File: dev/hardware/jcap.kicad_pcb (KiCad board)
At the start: 2 copper layers, 136.8 x 87 mm, 65 parts, among them J201 CPU PGMR, J202 SPARE CPU HDR, J203 GPU PGMR, J204 SPARE GPU HDR, J301 DC IN, J501 VGA OUT, J601 CONTROLS, Q301 IPP80P03P4L-04, SW201 CPU ~{RES}, SW202 DEBUG, SW203 GPU ~{RES}, SW601 TILT, U201 P8X32A-D40, U202 P8X32A-D40, U301 LF33_TO220, U401 24LC256, U402 24LC256, U601 74HC165, U602 74HC165, Y201 6.5MHz, Y202 6.5MHz

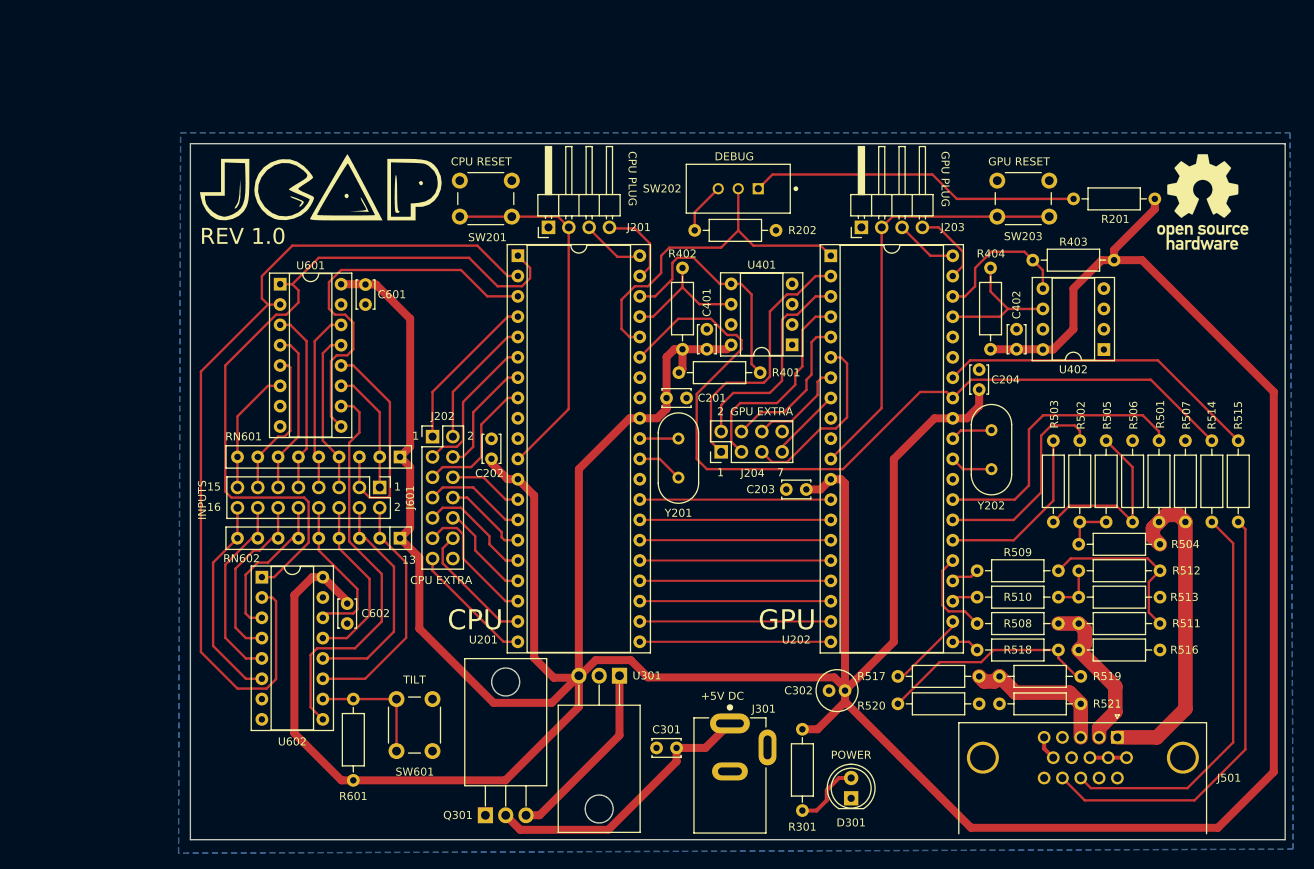
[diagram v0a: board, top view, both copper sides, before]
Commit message: Finalized silkscreen - now actually ready for prod
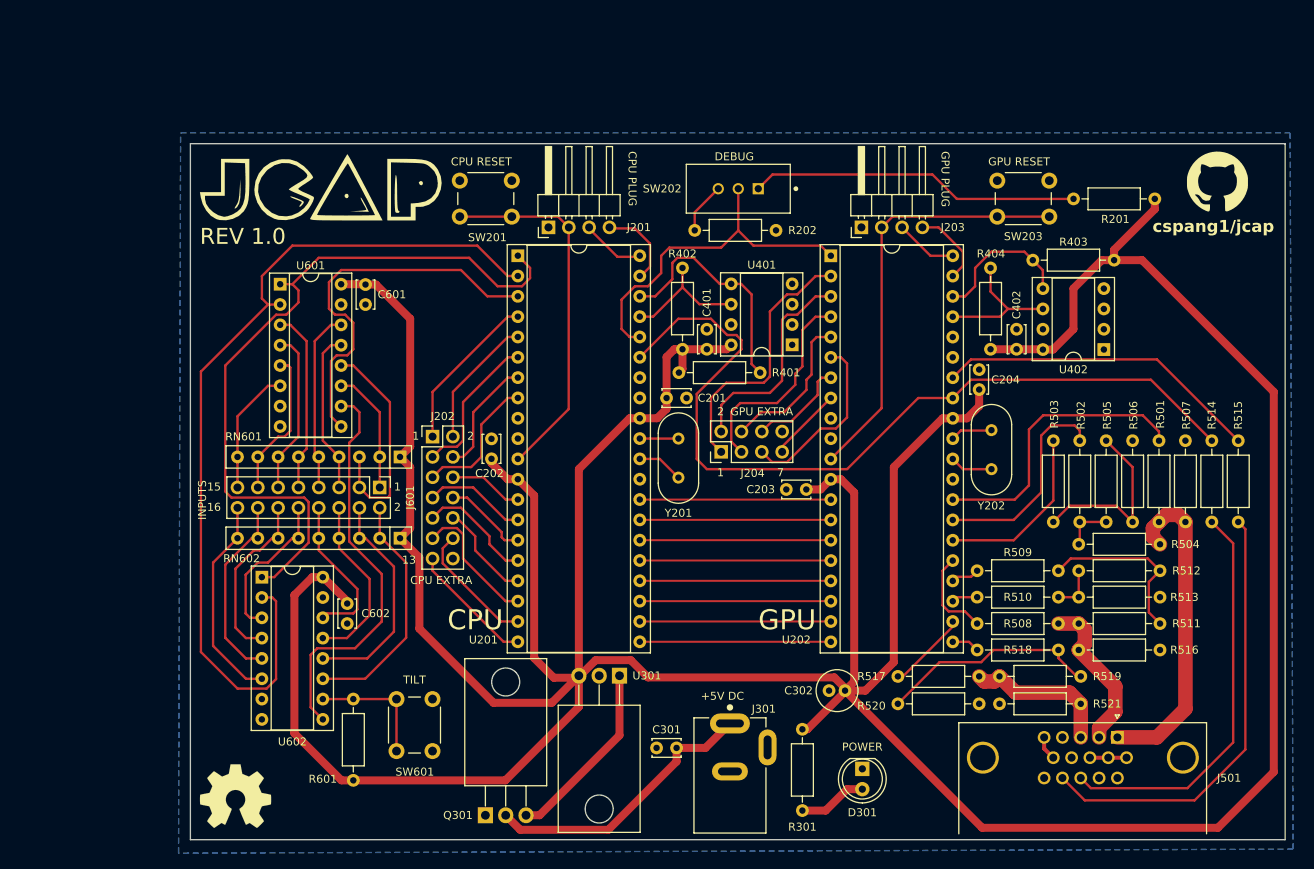
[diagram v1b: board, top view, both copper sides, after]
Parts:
- removed the REF** at (224.5, 73.3)
- added G***: LOGO, jcap-footprints:github_small, F.Cu at (226.4, 70.7)
- added REF**: OSHW-Symbol_8.9x8mm_SilkScreen, Symbol:OSHW-Symbol_8.9x8mm_SilkScreen, F.Cu at (103.6, 147.6)
- moved D301 3.94 mm to (182.0, 144.1), turned to -90 degrees
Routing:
- net BLUE1: track 10.1 -> 8.80 mm
- net +3.3V: track 534.6 -> 535.6 mm
- net /Propellers/GPU_SPARE_7: track 9.25 -> 8.61 mm
- net /Input/IN13: track 20.0 -> 19.4 mm
- net V_SYNC: track 106.3 -> 105.7 mm
- net /Propellers/CPU_SPARE_10: track 12.4 -> 11.9 mm
- net Net-(R518-Pad1): track 27.6 -> 27.1 mm
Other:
- board text added: "cspang1/jcap"

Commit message: Finalized dev board administrivia
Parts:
- R201, R202: value 200 -> 10K
- U201, U202: value P8X32A-D40 -> P8X32A
- U301: value LF33_TO220 -> LM3940IT
- moved R202 33.8 mm to (140.7, 62.2), turned to 0 degrees
- moved R515 32.0 mm to (208.7, 88.5), turned to -90 degrees
- moved D301 25.0 mm to (161.7, 129.5)
- moved C201 25.0 mm to (139.7, 83.2)
- moved J204 25.0 mm to (144.0, 89.9)
- moved R401 25.0 mm to (148.9, 80.0)
- moved R502 25.0 mm to (188.8, 98.7)
- moved R510 25.0 mm to (186.2, 108.1)
- moved R518 25.0 mm to (186.2, 114.7)
- moved SW203 25.0 mm to (178.5, 56.0)
- moved REF** 25.0 mm to (83.3, 133.0)
- moved J201 25.0 mm to (122.4, 61.9)
- moved J202 25.0 mm to (108.0, 88.0)
- moved R507 25.0 mm to (202.1, 88.5)
- moved R508 25.0 mm to (186.2, 111.4)
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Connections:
- R202 pad 1: GND -> Net-(R202-Pad1)
- R202 pad 2: Net-(R202-Pad2) -> GND
- R515 pad 1: Net-(J501-Pad14) -> H_SYNC
- R515 pad 2: H_SYNC -> Net-(J501-Pad14)
- SW202 pad 3: Net-(R202-Pad2) -> Net-(R202-Pad1)
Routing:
- net Net-(R202-Pad2): track 6.43 -> 0.00 mm
- net Net-(R202-Pad1): track 0.00 -> 6.43 mm
